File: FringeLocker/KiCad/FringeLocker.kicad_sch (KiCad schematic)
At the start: 32 parts, among them J1 OUT, J2 TP Scaler, J3 Conn_01x03_Male, SW1 NIDEC_SS-10-16, SW2 SW_Push_DPDT, U1 TL074

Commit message: Reorg of folders
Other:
- company: (none) -> ©Loic74650
- title: (none) -> Fringer Locker
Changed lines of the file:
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@@
 (kicad_sch (version 20211123) (generator eeschema)
   (paper "A4")
+  (title_block
+    (title "Fringer Locker")
+    (date "2023-02-10")
+    (rev "V1.0")
+    (company "©Loic74650")
+  )
   (junction (at 162.56 86.36) (diameter 0) (color 0 0 0 0)
   )

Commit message: updated Readme
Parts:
- added C?: 100nF, symbol Device:C
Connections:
- net at R2.1, R4.2, U1.6 (-): now also C?.2
- net at R1.1, R2.2, TP1.1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: now also C?.1
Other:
- note added: "Low pass filter. Adjust C value accordingly"
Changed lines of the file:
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@@
   (junction (at 213.36 121.92) (diameter 0) (color 0 0 0 0)
   )
+  (junction (at 80.01 71.12) (diameter 0) (color 0 0 0 0)
+  )
   (junction (at 96.52 85.09) (diameter 0) (color 0 0 0 0)
   )
   (junction (at 274.32 121.92) (diameter 0) (color 0 0 0 0)
+  )
+  (junction (at 96.52 71.12) (diameter 0) (color 0 0 0 0)
   )
   (junction (at 236.22 68.58) (diameter 0) (color 0 0 0 0)
@@
     (stroke (width 0) (type default) (color 0 0 0 0))
   )
+  (wire (pts (xy 80.01 71.12) (xy 80.01 59.69))
+    (stroke (width 0) (type default) (color 0 0 0 0))
+  )
   (wire (pts (xy 124.46 34.29) (xy 129.54 34.29))
     (stroke (width 0) (type default) (color 0 0 0 0))
@@
     (stroke (width 0) (type default) (color 0 0 0 0))
   )
+  (wire (pts (xy 96.52 59.69) (xy 96.52 71.12))
+    (stroke (width 0) (type default) (color 0 0 0 0))
+  )
   (wire (pts (xy 172.72 85.09) (xy 172.72 86.36))
     (stroke (width 0) (type default) (color 0 0 0 0))
@@
     (stroke (width 0) (type default) (color 0 0 0 0))
   )
+  (wire (pts (xy 80.01 59.69) (xy 83.82 59.69))
+    (stroke (width 0) (type default) (color 0 0 0 0))
+  )
   (wire (pts (xy 80.01 87.63) (xy 81.28 87.63))
     (stroke (width 0) (type default) (color 0 0 0 0))
   )
   (wire (pts (xy 227.33 123.19) (xy 227.33 120.65))
+    (stroke (width 0) (type default) (color 0 0 0 0))
+  )
+  (wire (pts (xy 91.44 59.69) (xy 96.52 59.69))
     (stroke (width 0) (type default) (color 0 0 0 0))
   )
@@
   (text "Prescaler" (at 156.21 39.37 0)
     (effects (font (size 3 3)) (justify left bottom))
+  )
+  (text "Low pass filter.\nAdjust C value accordingly" (at 77.47 48.26 0)
+    (effects (font (size 1.27 1.27)) (justify left bottom))
   )
   (symbol (lib_id "power:GND") (at 142.24 102.87 0) (unit 1)
@@
     (pin "4")
   )
+  (symbol (lib_id "Device:C") (at 87.63 59.69 90) (unit 1)
+    (in_bom yes) (on_board yes) (fields_autoplaced)
+    (property "Reference" "C?" (id 0) (at 87.63 52.07 90))
+    (property "Value" "100nF" (id 1) (at 87.63 54.61 90))
+    (property "Footprint" "" (id 2) (at 91.44 58.7248 0)
+      (effects (font (size 1.27 1.27)) hide)
+    )
+    (property "Datasheet" "~" (id 3) (at 87.63 59.69 0)
+      (effects (font (size 1.27 1.27)) hide)
+    )
+    (pin "1")
+    (pin "2")
+  )
   (symbol (lib_id "Device:R") (at 105.41 128.27 270) (unit 1)
     (in_bom yes) (on_board yes)
@@
       (reference "C6") (unit 1) (value "1uF") (footprint "Capacitor_SMD:C_0603_1608Metric_Pad1.08x0.95mm_HandSolder")
     )
+    (path "/7acd1ea0-a3cd-41e5-b164-3fb30010665b"
+      (reference "C?") (unit 1) (value "100nF") (footprint "")
+    )
     (path "/ac0aa4ae-94d8-4291-b223-afb5eabf93ed"

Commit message: V2.0
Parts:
- C?: value 100nF -> 300nF
- R2: value 22K -> 470K
- R6: value 1M -> 10M
- R7: value 100K -> 1M
- R8: value 10K -> 470K
- R9: value 1K -> 100K
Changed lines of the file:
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@@
     (title "Fringer Locker")
     (date "2023-02-10")
-    (rev "V1.0")
+    (rev "V2.0")
     (company "©Loic74650")
   )
@@
     (in_bom yes) (on_board yes)
     (property "Reference" "R2" (id 0) (at 87.63 68.58 90))
-    (property "Value" "22K" (id 1) (at 87.63 71.12 90))
+    (property "Value" "470K" (id 1) (at 87.63 71.12 90))
     (property "Footprint" "Resistor_SMD:R_0805_2012Metric_Pad1.20x1.40mm_HandSolder" (id 2) (at 87.63 69.342 90)
       (effects (font (size 1.27 1.27)) hide)
@@
     (in_bom yes) (on_board yes)
     (property "Reference" "R6" (id 0) (at 133.35 31.75 90))
-    (property "Value" "1M" (id 1) (at 133.35 34.29 90))
+    (property "Value" "10M" (id 1) (at 133.35 34.29 90))
     (property "Footprint" "Resistor_SMD:R_0805_2012Metric_Pad1.20x1.40mm_HandSolder" (id 2) (at 133.35 32.512 90)
       (effects (font (size 1.27 1.27)) hide)
@@
     (in_bom yes) (on_board yes)
     (property "Reference" "R9" (id 0) (at 133.35 71.12 90))
-    (property "Value" "1K" (id 1) (at 133.35 73.66 90))
+    (property "Value" "100K" (id 1) (at 133.35 73.66 90))
     (property "Footprint" "Resistor_SMD:R_0805_2012Metric_Pad1.20x1.40mm_HandSolder" (id 2) (at 133.35 71.882 90)
       (effects (font (size 1.27 1.27)) hide)
@@
     (in_bom yes) (on_board yes)
     (property "Reference" "R7" (id 0) (at 133.35 44.45 90))
-    (property "Value" "100K" (id 1) (at 133.35 46.99 90))
+    (property "Value" "1M" (id 1) (at 133.35 46.99 90))
     (property "Footprint" "Resistor_SMD:R_0805_2012Metric_Pad1.20x1.40mm_HandSolder" (id 2) (at 133.35 45.212 90)
       (effects (font (size 1.27 1.27)) hide)
@@
     (in_bom yes) (on_board yes) (fields_autoplaced)
     (property "Reference" "C?" (id 0) (at 87.63 52.07 90))
-    (property "Value" "100nF" (id 1) (at 87.63 54.61 90))
+    (property "Value" "300nF" (id 1) (at 87.63 54.61 90))
     (property "Footprint" "" (id 2) (at 91.44 58.7248 0)
       (effects (font (size 1.27 1.27)) hide)
@@
     (in_bom yes) (on_board yes)
     (property "Reference" "R8" (id 0) (at 133.35 57.15 90))
-    (property "Value" "10K" (id 1) (at 133.35 59.69 90))
+    (property "Value" "470K" (id 1) (at 133.35 59.69 90))
     (property "Footprint" "Resistor_SMD:R_0805_2012Metric_Pad1.20x1.40mm_HandSolder" (id 2) (at 133.35 57.912 90)
       (effects (font (size 1.27 1.27)) hide)
@@
     )
     (path "/7acd1ea0-a3cd-41e5-b164-3fb30010665b"
-      (reference "C?") (unit 1) (value "100nF") (footprint "")
+      (reference "C?") (unit 1) (value "300nF") (footprint "")
     )
     (path "/ac0aa4ae-94d8-4291-b223-afb5eabf93ed"
@@
     )
     (path "/00000000-0000-0000-0000-000063e88937"
-      (reference "R2") (unit 1) (value "22K") (footprint "Resistor_SMD:R_0805_2012Metric_Pad1.20x1.40mm_HandSolder")
+      (reference "R2") (unit 1) (value "470K") (footprint "Resistor_SMD:R_0805_2012Metric_Pad1.20x1.40mm_HandSolder")
     )
     (path "/ab22a256-6871-46d8-bba1-db51f1048842"
@@
     )
     (path "/00000000-0000-0000-0000-000063ec2a89"
-      (reference "R6") (unit 1) (value "1M") (footprint "Resistor_SMD:R_0805_2012Metric_Pad1.20x1.40mm_HandSolder")
+      (reference "R6") (unit 1) (value "10M") (footprint "Resistor_SMD:R_0805_2012Metric_Pad1.20x1.40mm_HandSolder")
     )
     (path "/4642b14b-b915-4260-81f8-51cbec113774"
-      (reference "R7") (unit 1) (value "100K") (footprint "Resistor_SMD:R_0805_2012Metric_Pad1.20x1.40mm_HandSolder")
+      (reference "R7") (unit 1) (value "1M") (footprint "Resistor_SMD:R_0805_2012Metric_Pad1.20x1.40mm_HandSolder")
     )
     (path "/c9dbf2d7-29a7-4a9c-85c6-aca8df795faf"
-      (reference "R8") (unit 1) (value "10K") (footprint "Resistor_SMD:R_0805_2012Metric_Pad1.20x1.40mm_HandSolder")
+      (reference "R8") (unit 1) (value "470K") (footprint "Resistor_SMD:R_0805_2012Metric_Pad1.20x1.40mm_HandSolder")
     )
     (path "/27f2faaf-6b34-499c-a17d-980ff616b7cc"
-      (reference "R9") (unit 1) (value "1K") (footprint "Resistor_SMD:R_0805_2012Metric_Pad1.20x1.40mm_HandSolder")
+      (reference "R9") (unit 1) (value "100K") (footprint "Resistor_SMD:R_0805_2012Metric_Pad1.20x1.40mm_HandSolder")
     )
     (path "/34267562-41e5-4c22-a990-a4ae2157f52a"

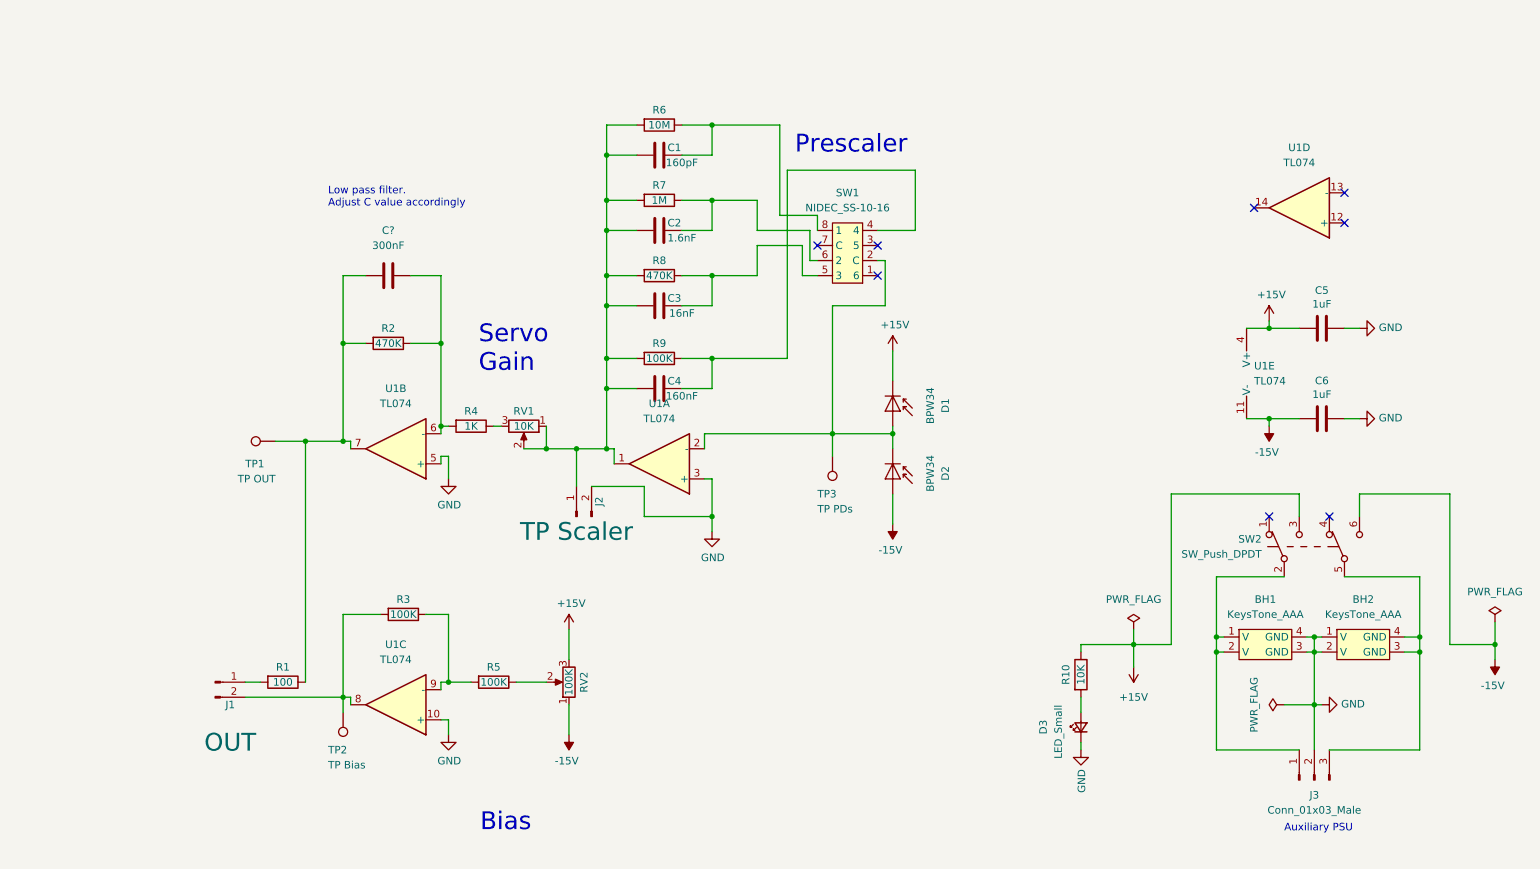
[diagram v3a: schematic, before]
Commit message: V3.0
Added  a x10 gain stage and a 2nd order adjustable low pass filter
Removed battery holders, requires external +/-15V to +/-18V supply
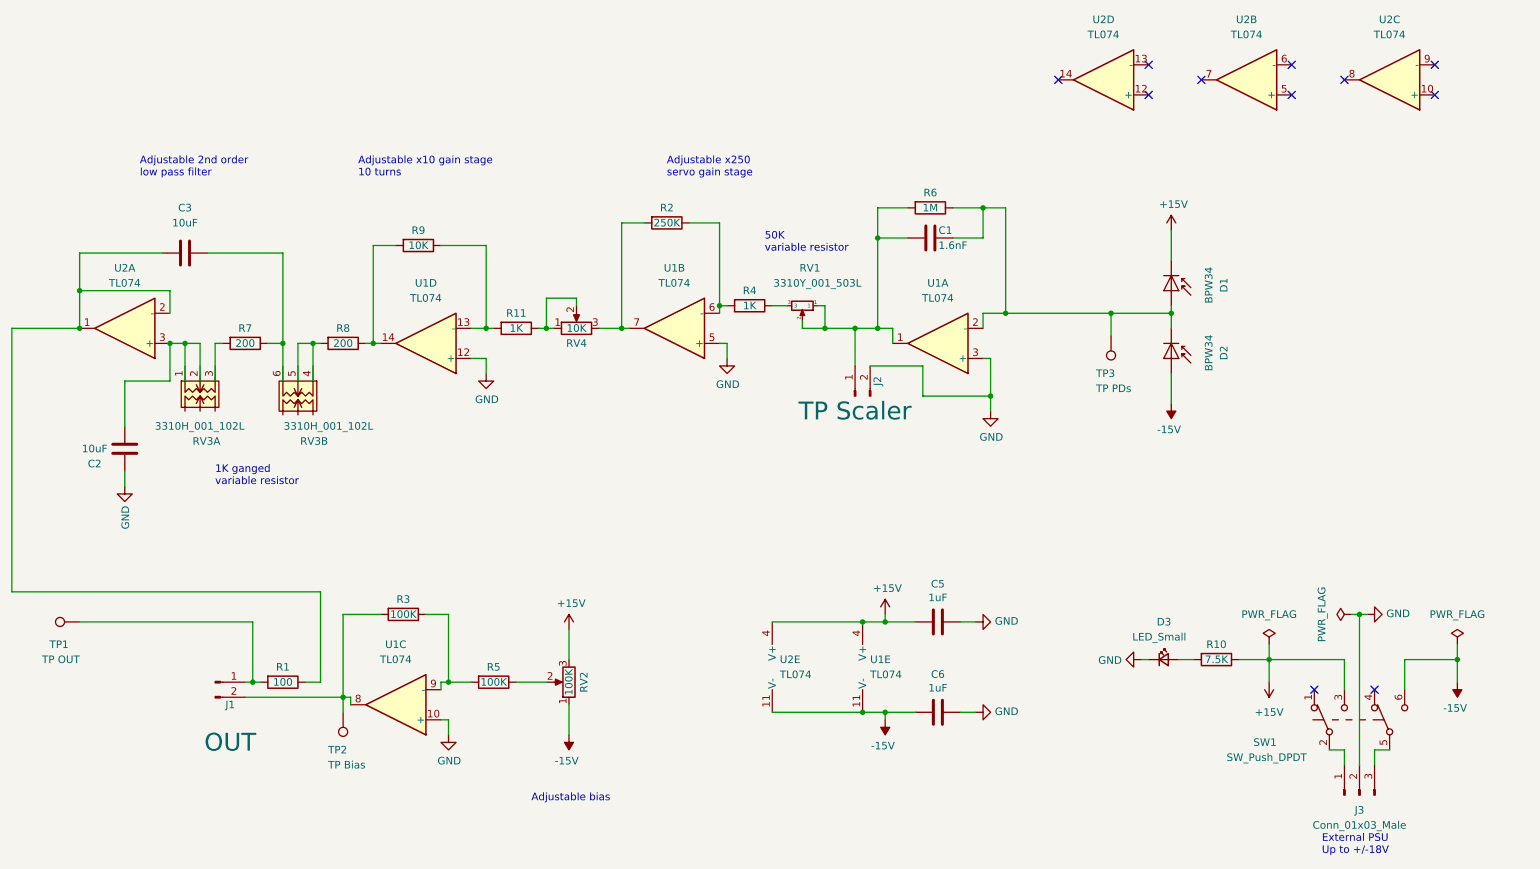
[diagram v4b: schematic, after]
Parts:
- removed BH1, BH2: KeysTone_AAA, BatteryHolder:Keystone_AAA, symbol My_Library:KeysTone_AAA
- removed C4: 160nF, Capacitor_SMD:C_0603_1608Metric_Pad1.08x0.95mm_HandSolder, symbol Device:C
- removed C?: 300nF, symbol Device:C
- removed RV1: 10K, Potentiometer_THT:Potentiometer_Bourns_3266W_Vertical, symbol FringeLocker-rescue:R_POT-Device
- removed SW1: NIDEC_SS-10-16, BatteryHolder:NIDEC_SS-10-16, symbol My_Library:NIDEC_SS-10-16
- removed SW2: SW_Push_DPDT, BatteryHolder:SlideSwitchASE_DPDT, symbol Switch:SW_Push_DPDT
- added R11: 1K, Resistor_SMD:R_0805_2012Metric_Pad1.20x1.40mm_HandSolder, symbol Device:R
- added RV1: 3310Y_001_503L, Bourns_3310H:Bourns3310Y, symbol Bourns3310:3310Y
- added RV3: 3310H_001_102L, Bourns_3310H:Bourns3310H, symbol Bourns3310:Bourns3310H_2
- added RV4: 10K, Potentiometer_THT:Potentiometer_Bourns_3266W_Vertical, symbol FringeLocker-rescue:R_POT-Device
- added SW1: SW_Push_DPDT, BatteryHolder:SlideSwitchASE_DPDT, symbol Switch:SW_Push_DPDT
- added U2: TL074, Package_SO:SO-14_5.3x10.2mm_P1.27mm, symbol Amplifier_Operational:TL074
- C1: value 160pF -> 1.6nF
- C2: value 1.6nF -> 10uF; footprint Capacitor_SMD:C_0603_1608Metric_Pad1.08x0.95mm_HandSolder -> Capacitor_SMD:C_1210_3225Metric_Pad1.33x2.70mm_HandSolder
- C3: value 16nF -> 10uF; footprint Capacitor_SMD:C_0603_1608Metric_Pad1.08x0.95mm_HandSolder -> Capacitor_SMD:C_1210_3225Metric_Pad1.33x2.70mm_HandSolder
- D3: footprint LED_SMD:LED_0402_1005Metric_Pad0.77x0.64mm_HandSolder -> LED_SMD:LED_0805_2012Metric_Pad1.15x1.40mm_HandSolder
- R10: value 10K -> 7.5K
- R2: value 470K -> 250K
- R6: value 10M -> 1M
- R7: value 1M -> 200
- R8: value 470K -> 200
- R9: value 100K -> 10K
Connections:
- net +15V: now also SW1.3 (C), U2.4 (V+)
- net -15V: now also SW1.6 (C), U2.11 (V-)
- net GND: now also C2.2, U1.12 (+)
- net at R4.1: now also RV1.3
- net at R2.2, U1.7: now also RV4.3; no longer R1.1, TP1.1
- net at J1.1 (Pin_1), R1.2: now also TP1.1
- net at C1.2, R6.1: now also D1.2 (A), D2.1 (K), TP3.1, U1.2 (-)
- net at R7.1: now also C3.1, RV3.6 (F); no longer C2.2
- net at R9.1: now also U1.13 (-), R11.2
- net at J3.1 (Pin_1): now also SW1.2 (B)
- net at J3.3 (Pin_3): now also SW1.5 (B)
- net at U1.14: now also R8.1, R9.2
- net at C3.2: now also R1.1, U2.1, U2.2 (-); no longer R8.1
- new net: C1.1, J2.1 (Pin_1), R6.2, RV1.1, RV1.2, U1.1
- new net: C2.1, RV3.1 (A), RV3.2 (B), U2.3 (+)
- new net: R7.2, RV3.3 (C)
- new net: R8.2, RV3.4 (D), RV3.5 (E)
- new net: R11.1, RV4.1, RV4.2
- no-connect marks 8 -> 11
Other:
- note added: "1K ganged variable resistor"
- note added: "50K variable resistor"
- note added: "Adjustable 2nd order low pass filter"
- note added: "Adjustable bias"
- note added: "Adjustable x10 gain stage 10 turns"
- note added: "Adjustable x250 servo gain stage"
- note added: "External PSU Up to +/-18V"
- note removed: "Auxiliary PSU"
- note removed: "Bias"
- note removed: "Low pass filter. Adjust C value accordingly"
- note removed: "Prescaler"
- note removed: "Servo Gain"
- moved on the sheet: C1, C5, C6, D1, D2, D3, J2, J3, R10, R2, R4, R6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
